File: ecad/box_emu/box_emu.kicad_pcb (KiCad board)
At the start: 2 copper layers, 4 parts

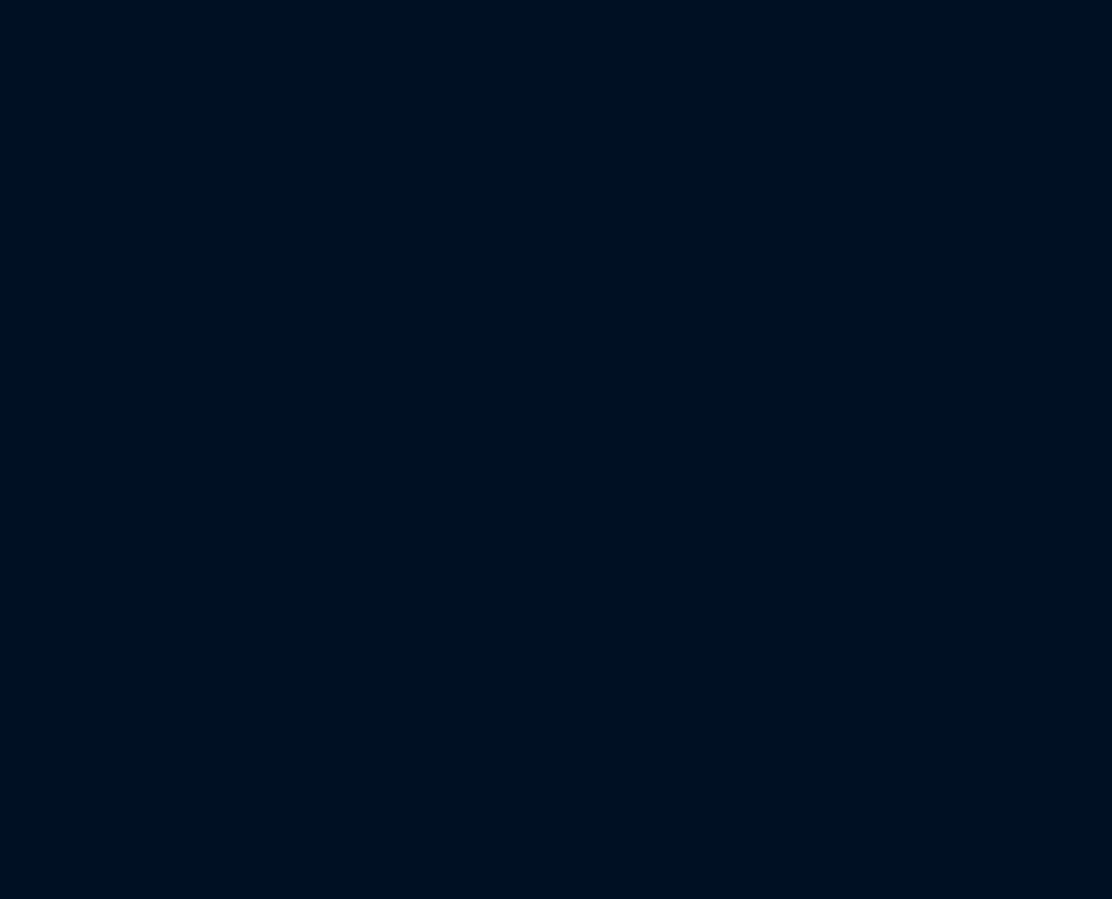
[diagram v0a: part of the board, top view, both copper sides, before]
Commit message: WIP fleshing out schematic for esp box emu pcb; added usb c port, mcp23017, ads1015, drv2605, battery charger, etc.
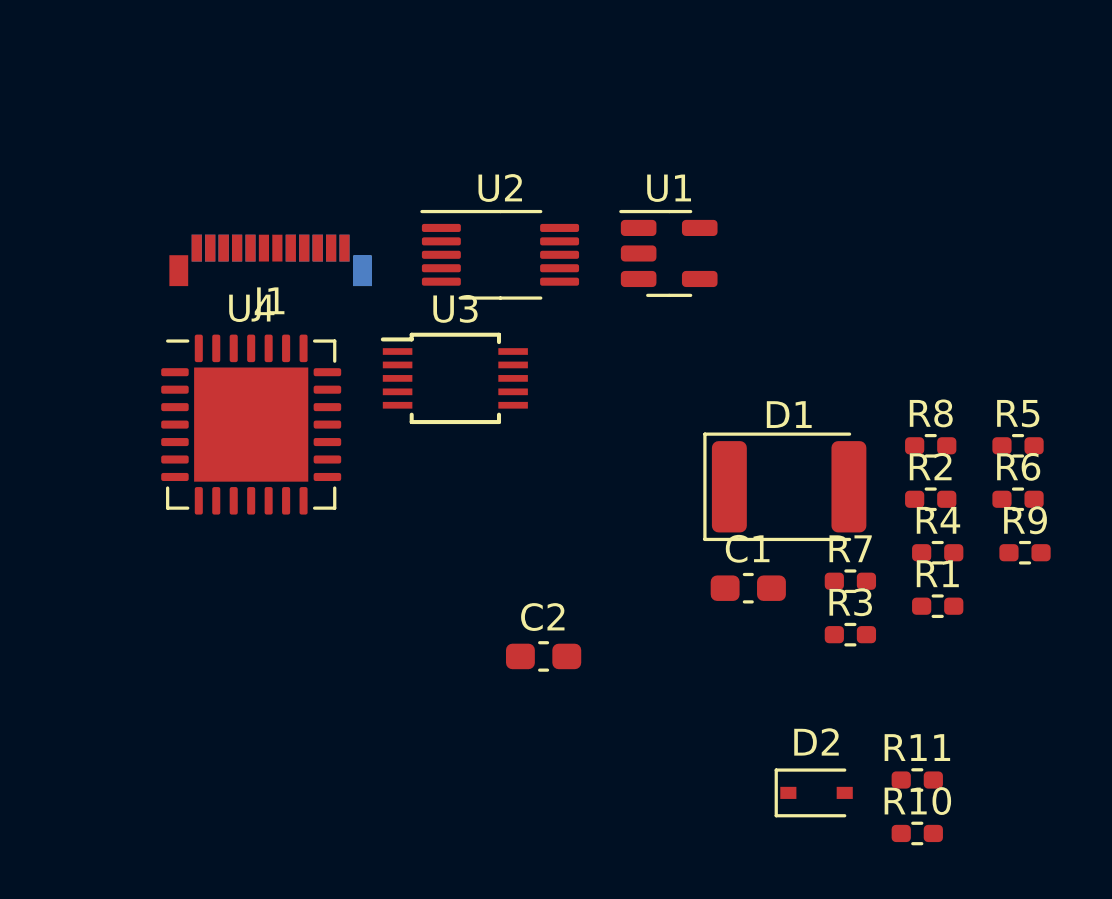
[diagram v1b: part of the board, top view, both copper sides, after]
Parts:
- added C1: 10uF, Capacitor_SMD:C_0603_1608Metric_Pad1.08x0.95mm_HandSolder, F.Cu at (154.9, 149.9)
- added C2: 1uF, Capacitor_SMD:C_0603_1608Metric_Pad1.08x0.95mm_HandSolder, F.Cu at (147.3, 152.4)
- added D1: LED, LED_SMD:LED_1812_4532Metric_Pad1.30x3.40mm_HandSolder, F.Cu at (156.5, 146.1)
- added D2: NSR0340HT1G, Diode_SMD:D_SOD-323, F.Cu at (157.5, 157.5)
- added J1: USB_C_Receptacle_USB2.0, Connector_USB:USB_C_Plug_Molex_105444, F.Cu at (137.2, 137.2)
- added R1: 2.0K, Resistor_SMD:R_0402_1005Metric_Pad0.72x0.64mm_HandSolder, F.Cu at (162.0, 150.5)
- added R10: 5.1K, Resistor_SMD:R_0402_1005Metric_Pad0.72x0.64mm_HandSolder, F.Cu at (161.2, 159.0)
- added R11: 5.1K, Resistor_SMD:R_0402_1005Metric_Pad0.72x0.64mm_HandSolder, F.Cu at (161.2, 157.0)
- added R2: 5.1K, Resistor_SMD:R_0402_1005Metric_Pad0.72x0.64mm_HandSolder, F.Cu at (161.7, 146.6)
- added R3: 10K, Resistor_SMD:R_0402_1005Metric_Pad0.72x0.64mm_HandSolder, F.Cu at (158.7, 151.6)
- added R4: 10K, Resistor_SMD:R_0402_1005Metric_Pad0.72x0.64mm_HandSolder, F.Cu at (162.0, 148.5)
- added R5: 10K, Resistor_SMD:R_0402_1005Metric_Pad0.72x0.64mm_HandSolder, F.Cu at (165.0, 144.6)
- added R6: 10K, Resistor_SMD:R_0402_1005Metric_Pad0.72x0.64mm_HandSolder, F.Cu at (165.0, 146.6)
- added R7: 10K, Resistor_SMD:R_0402_1005Metric_Pad0.72x0.64mm_HandSolder, F.Cu at (158.7, 149.6)
- added R8: 10K, Resistor_SMD:R_0402_1005Metric_Pad0.72x0.64mm_HandSolder, F.Cu at (161.7, 144.6)
- added R9: 10K, Resistor_SMD:R_0402_1005Metric_Pad0.72x0.64mm_HandSolder, F.Cu at (165.2, 148.5)
- added U1: MCP73831-2-OT, Package_TO_SOT_SMD:SOT-23-5, F.Cu at (152.0, 137.4)
- added U2: DRV2605LDGS, Package_SO:VSSOP-10_3x3mm_P0.5mm, F.Cu at (145.7, 137.4)
- added U3: ADS1015IDGS, Package_SO:TSSOP-10_3x3mm_P0.5mm, F.Cu at (144.0, 142.1)
- added U4: MCP23017_ML, Package_DFN_QFN:QFN-28-1EP_6x6mm_P0.65mm_EP4.25x4.25mm, F.Cu at (136.4, 143.8)
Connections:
- PMOD1 pad 3: unconnected-(PMOD1-Pad3) -> /USB D-
- PMOD1 pad 4: unconnected-(PMOD1-Pad4) -> /USB D+

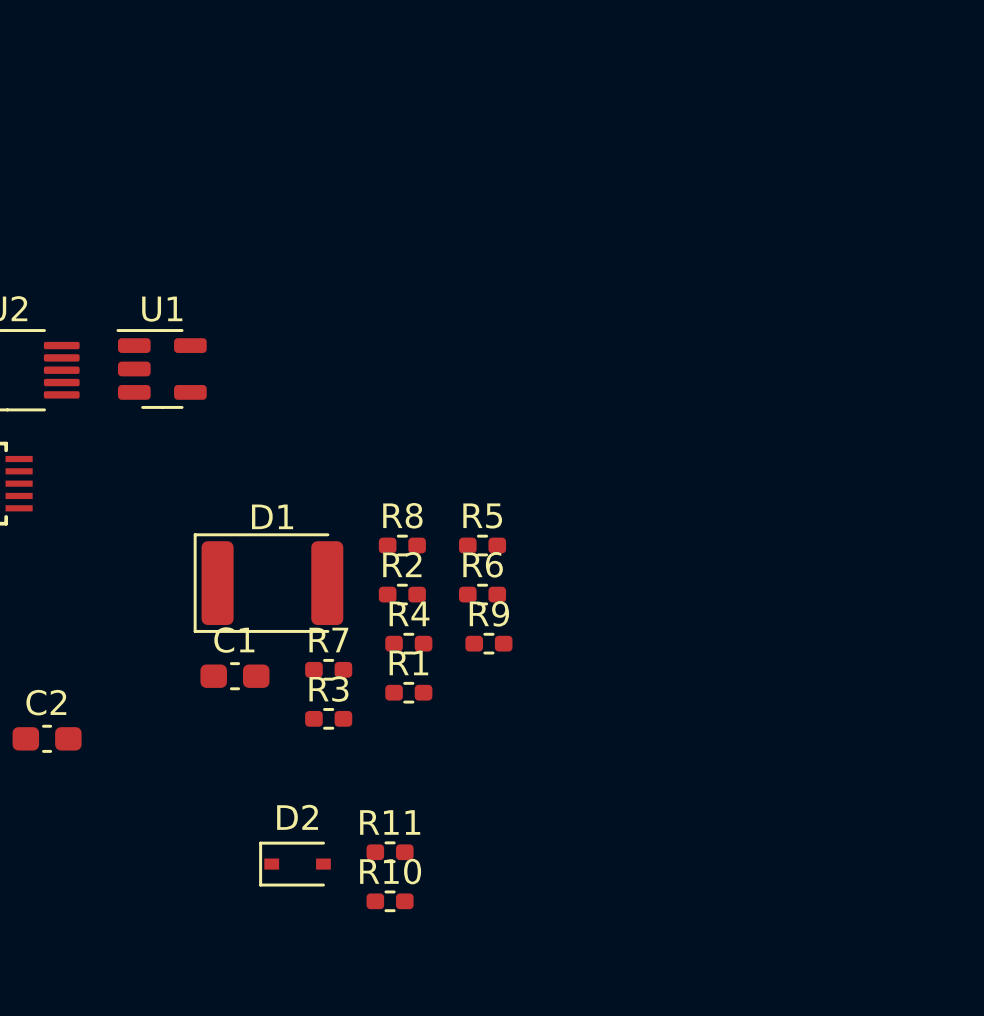
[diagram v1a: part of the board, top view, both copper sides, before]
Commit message: WIP fleshing out ecad some more - added buttons, 5v boost converter, and moved some things around.
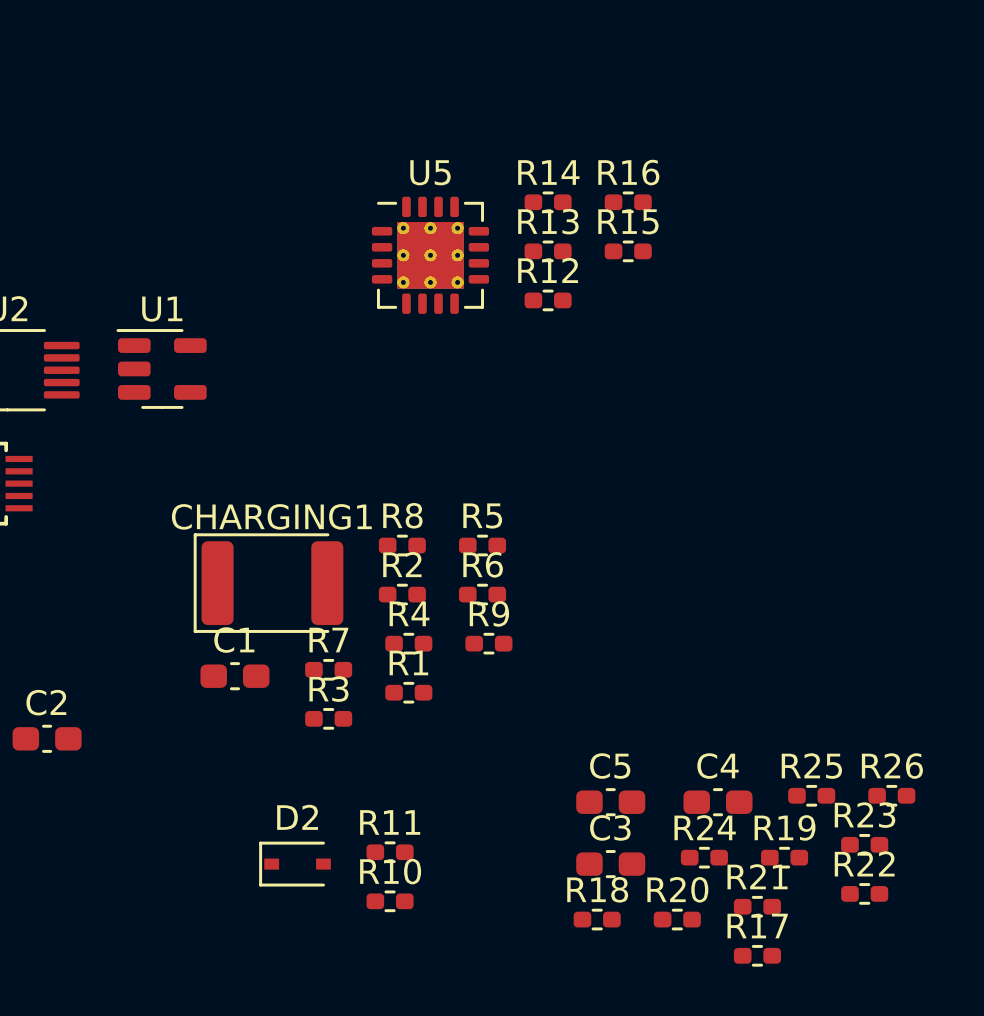
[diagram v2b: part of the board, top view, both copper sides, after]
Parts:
- added C3: .1uF, Capacitor_SMD:C_0603_1608Metric_Pad1.08x0.95mm_HandSolder, F.Cu at (170.2, 157.5)
- added C4: 10uF, Capacitor_SMD:C_0603_1608Metric_Pad1.08x0.95mm_HandSolder, F.Cu at (174.5, 155.0)
- added C5: 2.2uF, Capacitor_SMD:C_0603_1608Metric_Pad1.08x0.95mm_HandSolder, F.Cu at (170.2, 155.0)
- added R12: 1.87M, Resistor_SMD:R_0402_1005Metric_Pad0.72x0.64mm_HandSolder, F.Cu at (167.6, 134.6)
- added R13: 340K, Resistor_SMD:R_0402_1005Metric_Pad0.72x0.64mm_HandSolder, F.Cu at (167.6, 132.6)
- added R14: 200K, Resistor_SMD:R_0402_1005Metric_Pad0.72x0.64mm_HandSolder, F.Cu at (167.6, 130.6)
- added R15: 1.8M, Resistor_SMD:R_0402_1005Metric_Pad0.72x0.64mm_HandSolder, F.Cu at (170.9, 132.6)
- added R16: 200K, Resistor_SMD:R_0402_1005Metric_Pad0.72x0.64mm_HandSolder, F.Cu at (170.9, 130.6)
- added R17: 10K, Resistor_SMD:R_0402_1005Metric_Pad0.72x0.64mm_HandSolder, F.Cu at (176.1, 161.2)
- added R18: 10K, Resistor_SMD:R_0402_1005Metric_Pad0.72x0.64mm_HandSolder, F.Cu at (169.6, 159.7)
- added R19: 10K, Resistor_SMD:R_0402_1005Metric_Pad0.72x0.64mm_HandSolder, F.Cu at (177.2, 157.2)
- added R20: 10K, Resistor_SMD:R_0402_1005Metric_Pad0.72x0.64mm_HandSolder, F.Cu at (172.9, 159.7)
- added R21: 10K, Resistor_SMD:R_0402_1005Metric_Pad0.72x0.64mm_HandSolder, F.Cu at (176.1, 159.2)
- added R22: 10K, Resistor_SMD:R_0402_1005Metric_Pad0.72x0.64mm_HandSolder, F.Cu at (180.5, 158.7)
- added R23: 10K, Resistor_SMD:R_0402_1005Metric_Pad0.72x0.64mm_HandSolder, F.Cu at (180.5, 156.7)
- added R24: 10K, Resistor_SMD:R_0402_1005Metric_Pad0.72x0.64mm_HandSolder, F.Cu at (174.0, 157.2)
- added R25: 10K, Resistor_SMD:R_0402_1005Metric_Pad0.72x0.64mm_HandSolder, F.Cu at (178.3, 154.7)
- added R26: 10K, Resistor_SMD:R_0402_1005Metric_Pad0.72x0.64mm_HandSolder, F.Cu at (181.6, 154.7)
- added U5: TPS61092, Package_DFN_QFN:Texas_S-PVQFN-N16_EP2.7x2.7mm_ThermalVias, F.Cu at (162.9, 132.8)
- renumbered D1 to CHARGING1
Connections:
- CHARGING1 pad 2: +5V -> VBUS
- U1 pad 4: +5V -> VBUS
- U3 pad 4: unconnected-(U3-Pad4) -> /JOY_X
- U3 pad 5: unconnected-(U3-Pad5) -> /JOY_Y
- U4 pad 17: unconnected-(U4-Pad17) -> /UP
- U4 pad 18: unconnected-(U4-Pad18) -> /DOWN
- U4 pad 19: unconnected-(U4-Pad19) -> /LEFT
- U4 pad 20: unconnected-(U4-Pad20) -> /RIGHT
- U4 pad 21: unconnected-(U4-Pad21) -> /A
- U4 pad 22: unconnected-(U4-Pad22) -> /B
- U4 pad 23: unconnected-(U4-Pad23) -> /X
- U4 pad 24: unconnected-(U4-Pad24) -> /Y
- U4 pad 25: unconnected-(U4-Pad25) -> /START
- U4 pad 26: unconnected-(U4-Pad26) -> /SELECT
